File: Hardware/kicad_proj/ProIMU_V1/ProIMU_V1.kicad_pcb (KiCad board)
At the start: 2 copper layers, 50 x 50 mm, 37 parts, among them J1 USB4105-GF-A, J2 502570-0893, J3 Conn_01x01, J4 Conn_01x01, J5 Conn_01x01, J6 Conn_01x01, J7 Conn_01x01, U1 BMP280, U11 TJA1051T-3, U2 MPU-9250, U3 STM32F412CEU6, U4 AIR602

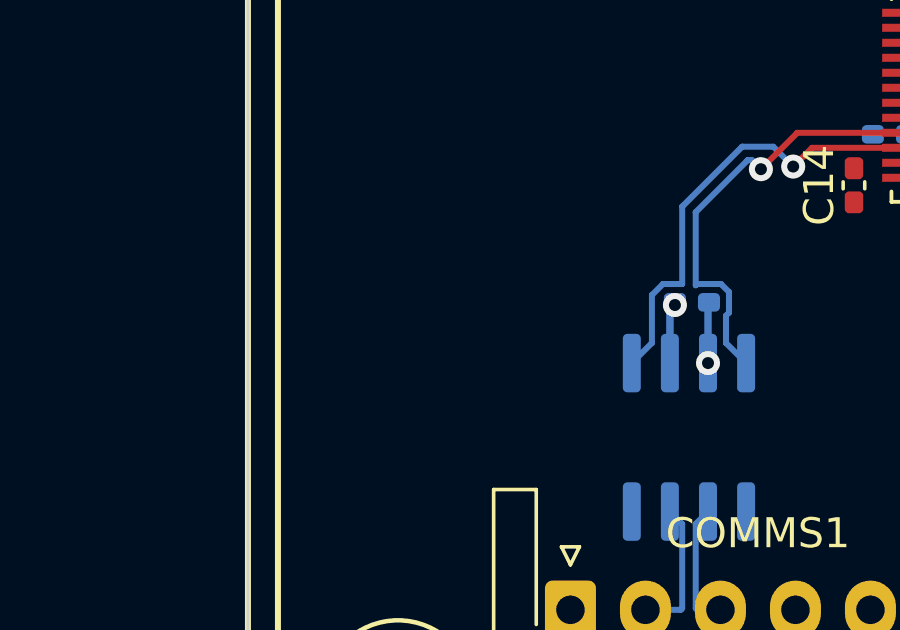
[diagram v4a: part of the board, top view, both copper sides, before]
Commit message: Update: Added CAN Transcreceiver
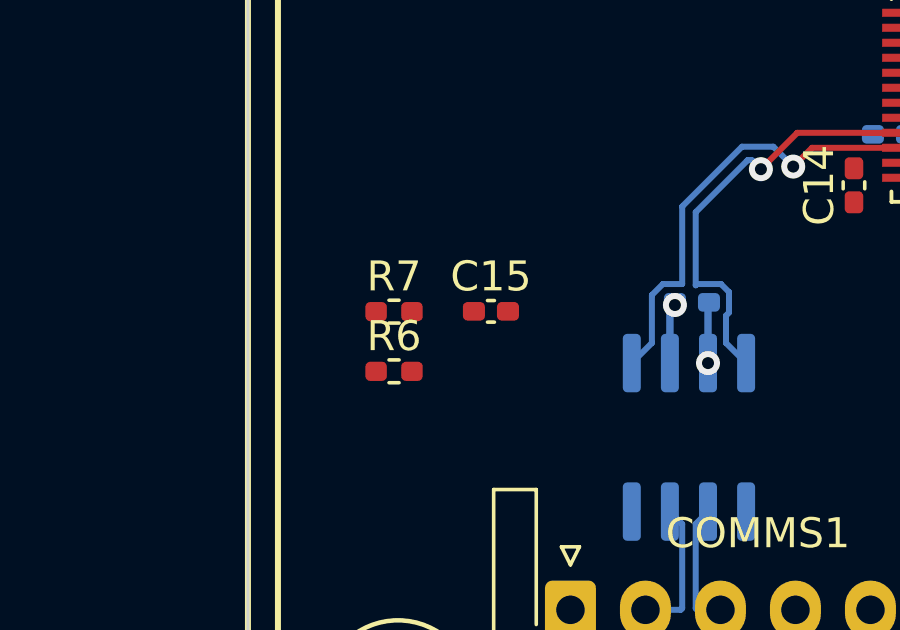
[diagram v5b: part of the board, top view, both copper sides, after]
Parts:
- added C15: 1uF, Capacitor_SMD:C_0402_1005Metric_Pad0.74x0.62mm_HandSolder, F.Cu at (131.6, 112.2)
- added R6: 2.2K, Resistor_SMD:R_0402_1005Metric_Pad0.72x0.64mm_HandSolder, F.Cu at (128.4, 114.2)
- added R7: 2.2K, Resistor_SMD:R_0402_1005Metric_Pad0.72x0.64mm_HandSolder, F.Cu at (128.4, 112.2)
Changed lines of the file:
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@@
   (net 65 "/CAN-")
   (net 66 "/CAN_SHUTDOWN")
+  (net 67 "Net-(C15-Pad2)")
+  (footprint "Resistor_SMD:R_0402_1005Metric_Pad0.72x0.64mm_HandSolder" (layer "F.Cu")
+    (at 128.37 114.2)
+    (descr "Resistor SMD 0402 (1005 Metric), square (rectangular) end terminal, IPC_7351 nominal with elongated pad for handsoldering. (Body size source: IPC-SM-782 page 72, https://www.pcb-3d.com/wordpress/wp-content/uploads/ipc-sm-782a_amendment_1_and_2.pdf), generated with kicad-footprint-generator")
+    (tags "resistor handsolder")
+    (property "Sheetfile" "ProIMU_V1.kicad_sch")
+    (property "Sheetname" "")
+    (attr smd)
+    (fp_text reference "R6" (at 0 -1.17) (layer "F.SilkS")
+      (effects (font (size 1 1) (thickness 0.15)))
+    )
+    (fp_text value "2.2K" (at 0 1.17) (layer "F.Fab")
+      (effects (font (size 1 1) (thickness 0.15)))
+    )
+    (fp_text user "${REFERENCE}" (at 0 0) (layer "F.Fab")
+      (effects (font (size 0.26 0.26) (thickness 0.04)))
+    )
+    (fp_line (start -0.167621 0.38) (end 0.167621 0.38) (layer "F.SilkS") (width 0.12))
+    (fp_line (start -0.167621 -0.38) (end 0.167621 -0.38) (layer "F.SilkS") (width 0.12))
+    (fp_line (start 1.1 -0.47) (end 1.1 0.47) (layer "F.CrtYd") (width 0.05))
+    (fp_line (start -1.1 0.47) (end -1.1 -0.47) (layer "F.CrtYd") (width 0.05))
+    (fp_line (start -1.1 -0.47) (end 1.1 -0.47) (layer "F.CrtYd") (width 0.05))
+    (fp_line (start 1.1 0.47) (end -1.1 0.47) (layer "F.CrtYd") (width 0.05))
+    (fp_line (start -0.525 0.27) (end -0.525 -0.27) (layer "F.Fab") (width 0.1))
+    (fp_line (start 0.525 0.27) (end -0.525 0.27) (layer "F.Fab") (width 0.1))
+    (fp_line (start -0.525 -0.27) (end 0.525 -0.27) (layer "F.Fab") (width 0.1))
+    (fp_line (start 0.525 -0.27) (end 0.525 0.27) (layer "F.Fab") (width 0.1))
+    (pad "1" smd roundrect (at -0.5975 0) (size 0.715 0.64) (layers "F.Cu" "F.Paste" "F.Mask") (roundrect_rratio 0.25)
+      (net 67 "Net-(C15-Pad2)") (pintype "passive"))
+    (pad "2" smd roundrect (at 0.5975 0) (size 0.715 0.64) (layers "F.Cu" "F.Paste" "F.Mask") (roundrect_rratio 0.25)
+      (net 64 "/CAN+") (pintype "passive"))
+    (model "${KICAD6_3DMODEL_DIR}/Resistor_SMD.3dshapes/R_0402_1005Metric.wrl"
+      (offset (xyz 0 0 0))
+      (scale (xyz 1 1 1))
+      (rotate (xyz 0 0 0))
+    )
+  )
   (footprint "footprints:AIR602" (layer "F.Cu")
     (at 158 122.5 180)
@@
     )
   )
+  (footprint "Resistor_SMD:R_0402_1005Metric_Pad0.72x0.64mm_HandSolder" (layer "F.Cu")
+    (at 128.37 112.21)
+    (descr "Resistor SMD 0402 (1005 Metric), square (rectangular) end terminal, IPC_7351 nominal with elongated pad for handsoldering. (Body size source: IPC-SM-782 page 72, https://www.pcb-3d.com/wordpress/wp-content/uploads/ipc-sm-782a_amendment_1_and_2.pdf), generated with kicad-footprint-generator")
+    (tags "resistor handsolder")
+    (property "Sheetfile" "ProIMU_V1.kicad_sch")
+    (property "Sheetname" "")
+    (attr smd)
+    (fp_text reference "R7" (at 0 -1.17) (layer "F.SilkS")
+      (effects (font (size 1 1) (thickness 0.15)))
+    )
+    (fp_text value "2.2K" (at 0 1.17) (layer "F.Fab")
+      (effects (font (size 1 1) (thickness 0.15)))
+    )
+    (fp_text user "${REFERENCE}" (at 0 0) (layer "F.Fab")
+      (effects (font (size 0.26 0.26) (thickness 0.04)))
+    )
+    (fp_line (start -0.167621 0.38) (end 0.167621 0.38) (layer "F.SilkS") (width 0.12))
+    (fp_line (start -0.167621 -0.38) (end 0.167621 -0.38) (layer "F.SilkS") (width 0.12))
+    (fp_line (start -1.1 0.47) (end -1.1 -0.47) (layer "F.CrtYd") (width 0.05))
+    (fp_line (start 1.1 -0.47) (end 1.1 0.47) (layer "F.CrtYd") (width 0.05))
+    (fp_line (start -1.1 -0.47) (end 1.1 -0.47) (layer "F.CrtYd") (width 0.05))
+    (fp_line (start 1.1 0.47) (end -1.1 0.47) (layer "F.CrtYd") (width 0.05))
+    (fp_line (start 0.525 0.27) (end -0.525 0.27) (layer "F.Fab") (width 0.1))
+    (fp_line (start -0.525 0.27) (end -0.525 -0.27) (layer "F.Fab") (width 0.1))
+    (fp_line (start -0.525 -0.27) (end 0.525 -0.27) (layer "F.Fab") (width 0.1))
+    (fp_line (start 0.525 -0.27) (end 0.525 0.27) (layer "F.Fab") (width 0.1))
+    (pad "1" smd roundrect (at -0.5975 0) (size 0.715 0.64) (layers "F.Cu" "F.Paste" "F.Mask") (roundrect_rratio 0.25)
+      (net 65 "/CAN-") (pintype "passive"))
+    (pad "2" smd roundrect (at 0.5975 0) (size 0.715 0.64) (layers "F.Cu" "F.Paste" "F.Mask") (roundrect_rratio 0.25)
+      (net 67 "Net-(C15-Pad2)") (pintype "passive"))
+    (model "${KICAD6_3DMODEL_DIR}/Resistor_SMD.3dshapes/R_0402_1005Metric.wrl"
+      (offset (xyz 0 0 0))
+      (scale (xyz 1 1 1))
+      (rotate (xyz 0 0 0))
+    )
+  )
   (footprint "Capacitor_SMD:C_0402_1005Metric_Pad0.74x0.62mm_HandSolder" (layer "F.Cu")
     (at 105.4325 176)
@@
       (offset (xyz 0 0 0))
       (scale (xyz 1 1 1))
+      (rotate (xyz 0 0 0))
+    )
+  )
+  (footprint "Capacitor_SMD:C_0402_1005Metric_Pad0.74x0.62mm_HandSolder" (layer "F.Cu")
+    (at 131.6 112.2)
+    (descr "Capacitor SMD 0402 (1005 Metric), square (rectangular) end terminal, IPC_7351 nominal with elongated pad for handsoldering. (Body size source: IPC-SM-782 page 76, https://www.pcb-3d.com/wordpress/wp-content/uploads/ipc-sm-782a_amendment_1_and_2.pdf), generated with kicad-footprint-generator")
+    (tags "capacitor handsolder")
+    (property "Sheetfile" "ProIMU_V1.kicad_sch")
+    (property "Sheetname" "")
+    (attr smd)
+    (fp_text reference "C15" (at 0 -1.16) (layer "F.SilkS")
+      (effects (font (size 1 1) (thickness 0.15)))
+    )
+    (fp_text value "1uF" (at 0 1.16) (layer "F.Fab")
+      (effects (font (size 1 1) (thickness 0.15)))
+    )
+    (fp_text user "${REFERENCE}" (at 0 0) (layer "F.Fab")
+      (effects (font (size 0.25 0.25) (thickness 0.04)))
+    )
+    (fp_line (start -0.115835 0.36) (end 0.115835 0.36) (layer "F.SilkS") (width 0.12))
+    (fp_line (start -0.115835 -0.36) (end 0.115835 -0.36) (layer "F.SilkS") (width 0.12))
+    (fp_line (start 1.08 0.46) (end -1.08 0.46) (layer "F.CrtYd") (width 0.05))
+    (fp_line (start -1.08 -0.46) (end 1.08 -0.46) (layer "F.CrtYd") (width 0.05))
+    (fp_line (start 1.08 -0.46) (end 1.08 0.46) (layer "F.CrtYd") (width 0.05))
+    (fp_line (start -1.08 0.46) (end -1.08 -0.46) (layer "F.CrtYd") (width 0.05))
+    (fp_line (start -0.5 0.25) (end -0.5 -0.25) (layer "F.Fab") (width 0.1))
+    (fp_line (start -0.5 -0.25) (end 0.5 -0.25) (layer "F.Fab") (width 0.1))
+    (fp_line (start 0.5 -0.25) (end 0.5 0.25) (layer "F.Fab") (width 0.1))
+    (fp_line (start 0.5 0.25) (end -0.5 0.25) (layer "F.Fab") (width 0.1))
+    (pad "1" smd roundrect (at -0.5675 0) (size 0.735 0.62) (layers "F.Cu" "F.Paste" "F.Mask") (roundrect_rratio 0.25)
+      (net 2 "GND") (pintype "passive"))
+    (pad "2" smd roundrect (at 0.5675 0) (size 0.735 0.62) (layers "F.Cu" "F.Paste" "F.Mask") (roundrect_rratio 0.25)
+      (net 67 "Net-(C15-Pad2)") (pintype "passive"))
+    (model "${KICAD6_3DMODEL_DIR}/Capacitor_SMD.3dshapes/C_0402_1005Metric.wrl"
+      (offset (xyz 0 0 0))
+      (scale (xyz 1 1 1))
